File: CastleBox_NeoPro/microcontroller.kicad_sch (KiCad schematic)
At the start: 27 parts, among them J6 Conn_02x20_Odd_Even, SW1 SW_Push, U3 RP2350_60QFN, U4 ZD25WQ32CEIGR, Y1 12MHz

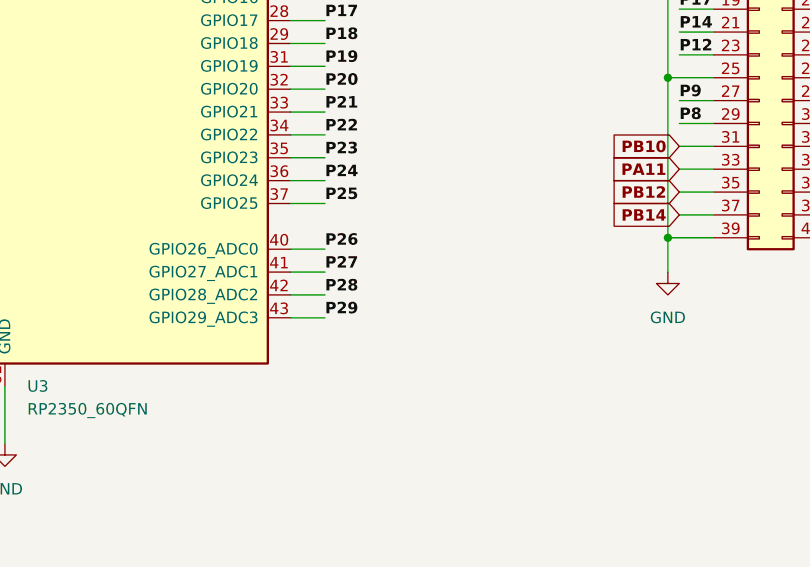
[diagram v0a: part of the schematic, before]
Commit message: added SPI communication protocol
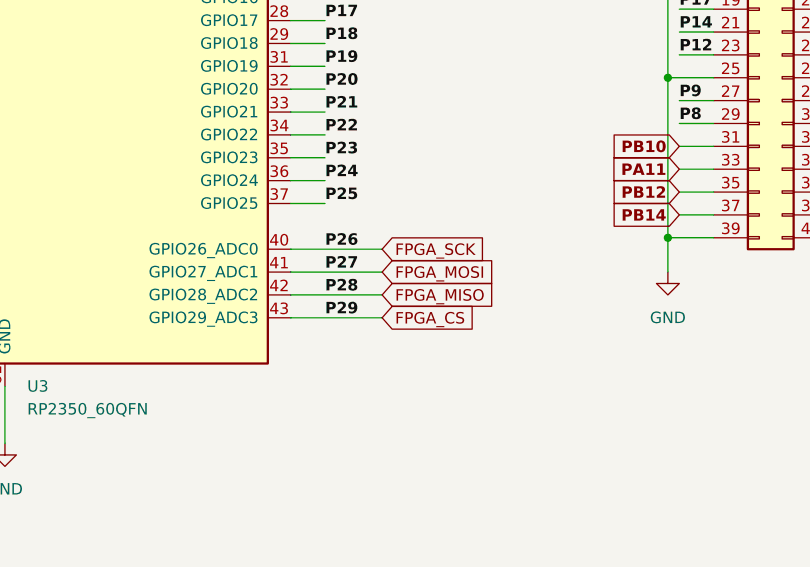
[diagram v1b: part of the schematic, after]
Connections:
- net P26 renamed FPGA_SCK
- net P27 renamed FPGA_MOSI
- net P28 renamed FPGA_MISO
- net P29 renamed FPGA_CS
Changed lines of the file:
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@@
 	(wire
 		(pts
-			(xy 172.72 140.97) (xy 168.91 140.97)
+			(xy 168.91 140.97) (xy 179.07 140.97)
 		)
 		(stroke
@@
 	(wire
 		(pts
-			(xy 172.72 135.89) (xy 168.91 135.89)
+			(xy 168.91 135.89) (xy 179.07 135.89)
 		)
 		(stroke
@@
 	(wire
 		(pts
-			(xy 172.72 138.43) (xy 168.91 138.43)
+			(xy 168.91 138.43) (xy 179.07 138.43)
 		)
 		(stroke
@@
 	(wire
 		(pts
-			(xy 172.72 143.51) (xy 168.91 143.51)
+			(xy 168.91 143.51) (xy 179.07 143.51)
 		)
 		(stroke
@@
 			)
 			(justify left bottom)
+		)
+	)
+	(global_label "FPGA_SCK"
+		(shape input)
+		(at 179.07 135.89 0)
+		(fields_autoplaced yes)
+		(effects
+			(font
+				(size 1.27 1.27)
+			)
+			(justify left)
+		)
+		(property "Intersheetrefs" "${INTERSHEET_REFS}"
+			(at 192.6422 135.89 0)
+			(effects
+				(font
+					(size 1.27 1.27)
+				)
+				(justify left)
+				(hide yes)
+			)
 		)
 	)
@@
 		)
 	)
+	(global_label "FPGA_MISO"
+		(shape input)
+		(at 179.07 140.97 0)
+		(fields_autoplaced yes)
+		(effects
+			(font
+				(size 1.27 1.27)
+			)
+			(justify left)
+		)
+		(property "Intersheetrefs" "${INTERSHEET_REFS}"
+			(at 193.5728 140.97 0)
+			(effects
+				(font
+					(size 1.27 1.27)
+				)
+				(justify left)
+				(hide yes)
+			)
+		)
+	)
 	(global_label "PA14"
 		(shape input)
@@
 		)
 	)
+	(global_label "FPGA_CS"
+		(shape input)
+		(at 179.07 143.51 0)
+		(fields_autoplaced yes)
+		(effects
+			(font
+				(size 1.27 1.27)
+			)
+			(justify left)
+		)
+		(property "Intersheetrefs" "${INTERSHEET_REFS}"
+			(at 191.3444 143.51 0)
+			(effects
+				(font
+					(size 1.27 1.27)
+				)
+				(justify left)
+				(hide yes)
+			)
+		)
+	)
 	(global_label "PA12"
 		(shape input)
@@
 			(effects
 				(font
+					(size 1.27 1.27)
+				)
+				(justify left)
+				(hide yes)
+			)
+		)
+	)
+	(global_label "FPGA_MOSI"
+		(shape input)
+		(at 179.07 138.43 0)
+		(fields_autoplaced yes)
+		(effects
+			(font
+				(size 1.27 1.27)
+			)
+			(justify left)
+		)
+		(property "Intersheetrefs" "${INTERSHEET_REFS}"
+			(at 193.5728 138.43 0)
+			(effects
+				(font
